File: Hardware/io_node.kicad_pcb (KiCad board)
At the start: 2 copper layers, 60 x 90 mm, 135 parts, among them J1 Conn_01x09, J10 Conn_01x04, J2 Conn_01x09, J3 Conn_01x09, J4 Conn_01x05, J5 USB_B_Micro, J6 Conn_01x05, J7 Conn_01x05, J8 Conn_01x02, J9 Conn_01x04, Q1 2N7002, Q2 2N7002, Q3 2N7002, Q4 2N7002, Q5 2N7002, Q6 2N7002, Q7 2N7002, Q8 2N7002, U1 STM32F103RBT6, U10 EL357N-G, U11 EL357N-G, U12 EL357N-G, U13 EL357N-G, U14 EL357N-G, U15 USBLC6-2SC6, U2 AMS1117-5.0, U3 AMS1117-3.3, U4 SP3485EN, U5 LM324DT, U6 LM324DT, U7 EL357N-G, U8 EL357N-G, U9 EL357N-G, Y1 8 MHz

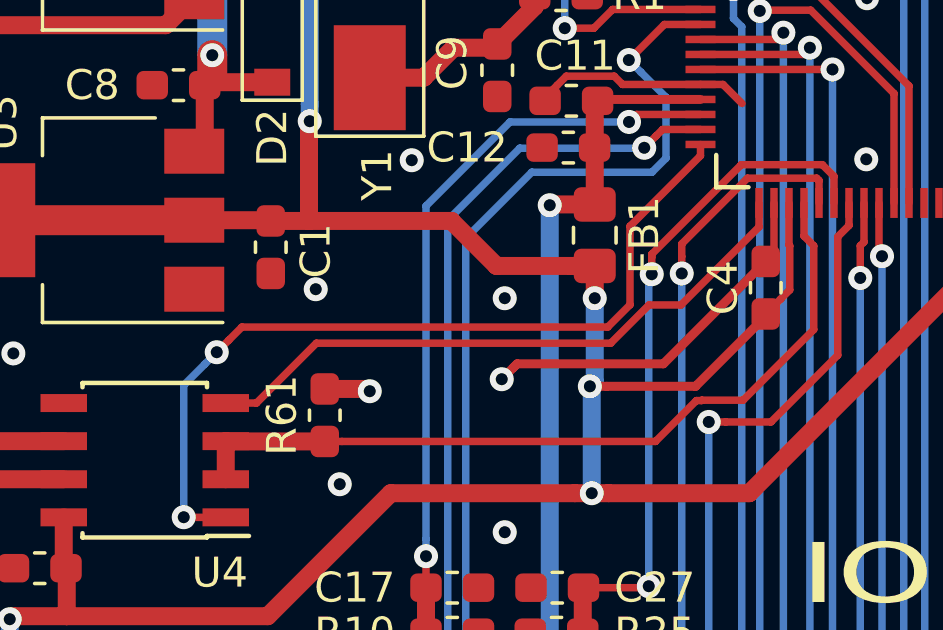
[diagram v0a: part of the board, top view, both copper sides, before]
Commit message: RS485 TX and RX was incorrect
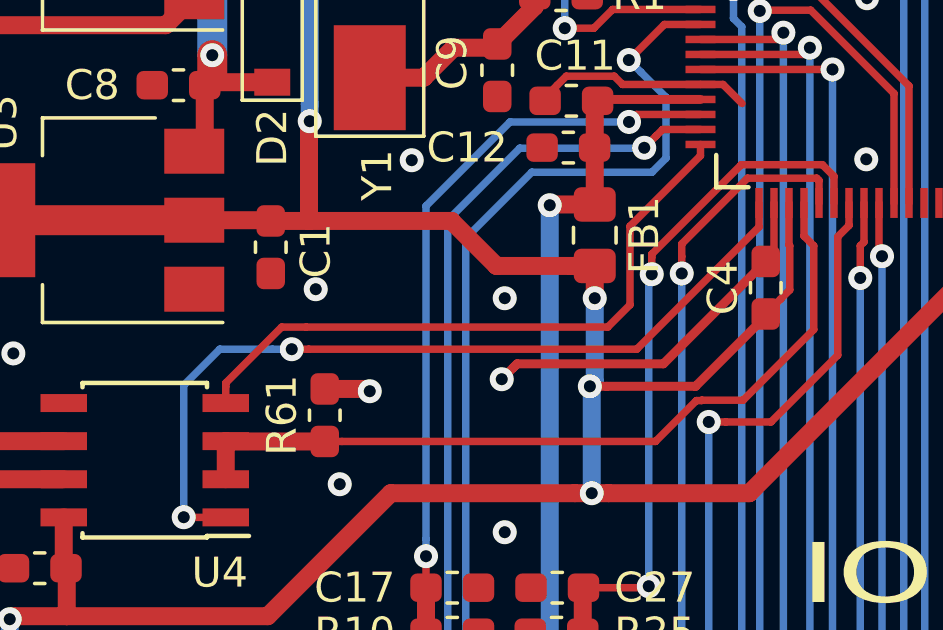
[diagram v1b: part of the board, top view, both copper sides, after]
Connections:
- U4 pad 1: /USART2_TX -> /USART2_RX
- U4 pad 4: /USART2_RX -> /USART2_TX
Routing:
- net /USART2_RX: track 21.0 -> 28.0 mm, vias 0 -> 2
- net /USART2_TX: track 28.1 -> 21.5 mm, vias 2 -> 0
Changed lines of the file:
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@@
     (fp_line (start -2.075 -2.525) (end -3.475 -2.525) (layer F.SilkS) (width 0.15))
     (pad 1 smd rect (at -2.7 -1.905 180) (size 1.55 0.6) (layers F.Cu F.Paste F.Mask)
-      (net 19 /USART2_TX))
+      (net 20 /USART2_RX))
     (pad 2 smd rect (at -2.7 -0.635 180) (size 1.55 0.6) (layers F.Cu F.Paste F.Mask)
       (net 21 /USART2_DE))
@@
       (net 21 /USART2_DE))
     (pad 4 smd rect (at -2.7 1.905 180) (size 1.55 0.6) (layers F.Cu F.Paste F.Mask)
-      (net 20 /USART2_RX))
+      (net 19 /USART2_TX))
     (pad 5 smd rect (at 2.7 1.905 180) (size 1.55 0.6) (layers F.Cu F.Paste F.Mask)
       (net 1 GND))
@@
   (segment (start 51.64 45.865) (end 51.25 45.475) (width 0.6) (layer F.Cu) (net 18))
   (segment (start 54.3 45.865) (end 51.64 45.865) (width 0.6) (layer F.Cu) (net 18))
-  (segment (start 58.305 48.405) (end 58.3 48.4) (width 0.25) (layer F.Cu) (net 19))
-  (segment (start 59.7 48.405) (end 58.305 48.405) (width 0.25) (layer F.Cu) (net 19))
-  (via (at 58.3 48.4) (size 0.8) (drill 0.4) (layers F.Cu B.Cu) (net 19))
-  (via (at 59.4 42.9) (size 0.8) (drill 0.4) (layers F.Cu B.Cu) (net 19))
-  (segment (start 75.525001 36.350001) (end 73.175172 38.69983) (width 0.25) (layer F.Cu) (net 19))
-  (segment (start 59.799999 42.500001) (end 59.4 42.9) (width 0.25) (layer F.Cu) (net 19))
-  (segment (start 60.237339 42.062661) (end 59.799999 42.500001) (width 0.25) (layer F.Cu) (net 19))
-  (segment (start 58.3 48.4) (end 58.3 44) (width 0.25) (layer B.Cu) (net 19))
-  (segment (start 59.000001 43.299999) (end 59.4 42.9) (width 0.25) (layer B.Cu) (net 19))
-  (segment (start 72.433131 42.062661) (end 60.237339 42.062661) (width 0.25) (layer F.Cu) (net 19))
   (segment (start 75.525001 35.975001) (end 75.525001 36.350001) (width 0.25) (layer F.Cu) (net 19))
-  (segment (start 73.175172 38.69983) (end 73.175172 41.32062) (width 0.25) (layer F.Cu) (net 19))
+  (segment (start 72.433131 42.062661) (end 62.38103 42.062661) (width 0.25) (layer F.Cu) (net 19))
   (segment (start 73.175172 41.32062) (end 72.433131 42.062661) (width 0.25) (layer F.Cu) (net 19))
-  (segment (start 58.3 44) (end 59.000001 43.299999) (width 0.25) (layer B.Cu) (net 19))
-  (segment (start 60.725 44.595) (end 59.7 44.595) (width 0.25) (layer F.Cu) (net 20))
-  (segment (start 62.72 42.6) (end 60.725 44.595) (width 0.25) (layer F.Cu) (net 20))
-  (segment (start 73.807225 41.324977) (end 72.532203 42.6) (width 0.25) (layer F.Cu) (net 20))
-  (segment (start 77.475001 38.724999) (end 74.875023 41.324977) (width 0.25) (layer F.Cu) (net 20))
+  (segment (start 73.175172 38.69983) (end 73.175172 41.32062) (width 0.25) (layer F.Cu) (net 19))
+  (segment (start 75.525001 36.350001) (end 73.175172 38.69983) (width 0.25) (layer F.Cu) (net 19))
+  (segment (start 59.7 44.045) (end 59.7 44.595) (width 0.25) (layer F.Cu) (net 19))
+  (segment (start 59.7 43.926998) (end 59.7 44.045) (width 0.25) (layer F.Cu) (net 19))
+  (segment (start 61.564337 42.062661) (end 59.7 43.926998) (width 0.25) (layer F.Cu) (net 19))
+  (segment (start 62.38103 42.062661) (end 61.564337 42.062661) (width 0.25) (layer F.Cu) (net 19))
+  (segment (start 59.7 48.405) (end 58.305 48.405) (width 0.25) (layer F.Cu) (net 20))
+  (segment (start 58.305 48.405) (end 58.3 48.4) (width 0.25) (layer F.Cu) (net 20))
+  (via (at 58.3 48.4) (size 0.8) (drill 0.4) (layers F.Cu B.Cu) (net 20))
+  (via (at 61.9 42.8) (size 0.8) (drill 0.4) (layers F.Cu B.Cu) (net 20))
   (segment (start 77.475001 37.925001) (end 77.475001 38.724999) (width 0.25) (layer F.Cu) (net 20))
-  (segment (start 74.875023 41.324977) (end 73.807225 41.324977) (width 0.25) (layer F.Cu) (net 20))
-  (segment (start 72.532203 42.6) (end 62.72 42.6) (width 0.25) (layer F.Cu) (net 20))
+  (segment (start 77.475001 38.724999) (end 73.4 42.8) (width 0.25) (layer F.Cu) (net 20))
+  (segment (start 62.465685 42.8) (end 61.9 42.8) (width 0.25) (layer F.Cu) (net 20))
+  (segment (start 73.4 42.8) (end 62.465685 42.8) (width 0.25) (layer F.Cu) (net 20))
+  (segment (start 61.25 42.8) (end 61.9 42.8) (width 0.25) (layer B.Cu) (net 20))
+  (segment (start 59.5 42.8) (end 61.25 42.8) (width 0.25) (layer B.Cu) (net 20))
+  (segment (start 58.3 48.4) (end 58.3 44) (width 0.25) (layer B.Cu) (net 20))
+  (segment (start 58.3 44) (end 59.5 42.8) (width 0.25) (layer B.Cu) (net 20))
   (segment (start 59.7 45.865) (end 59.7 47.135) (width 0.6) (layer F.Cu) (net 21))
   (segment (start 59.71 45.875) (end 59.7 45.865) (width 0.6) (layer F.Cu) (net 21))

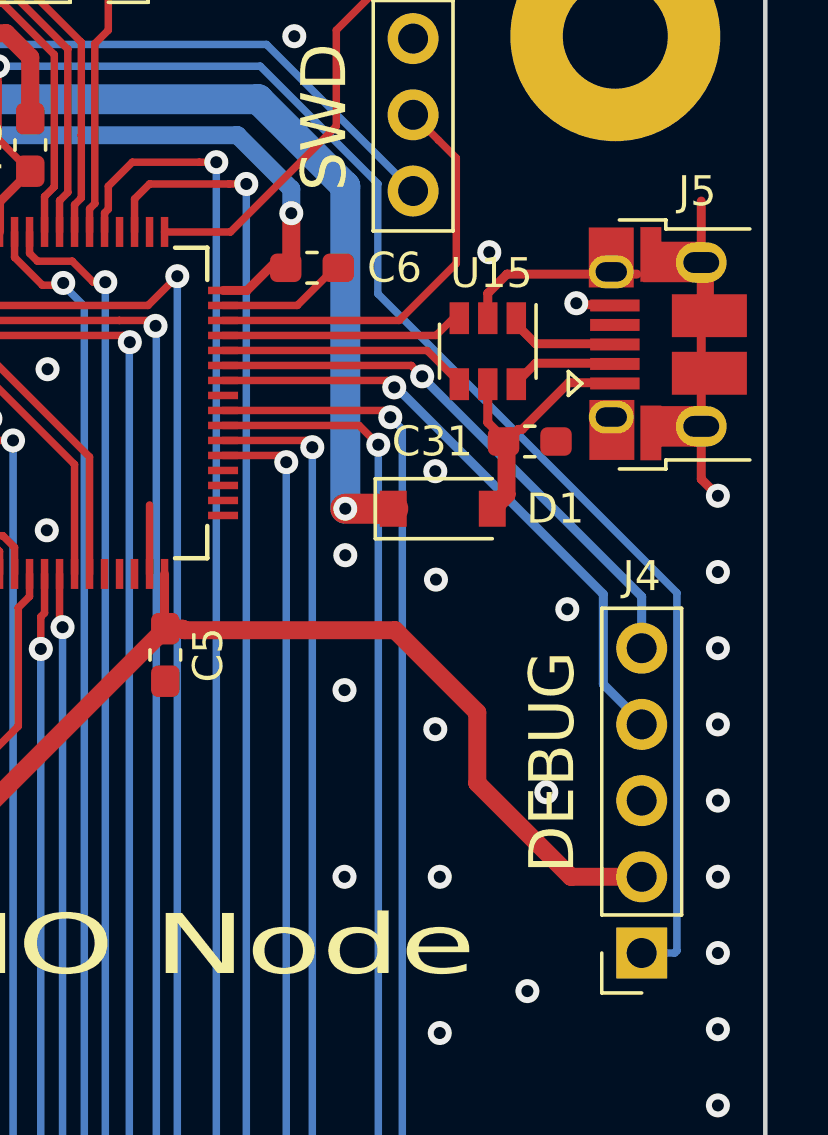
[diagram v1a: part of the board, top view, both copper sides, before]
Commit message: Debug RX TX swapped
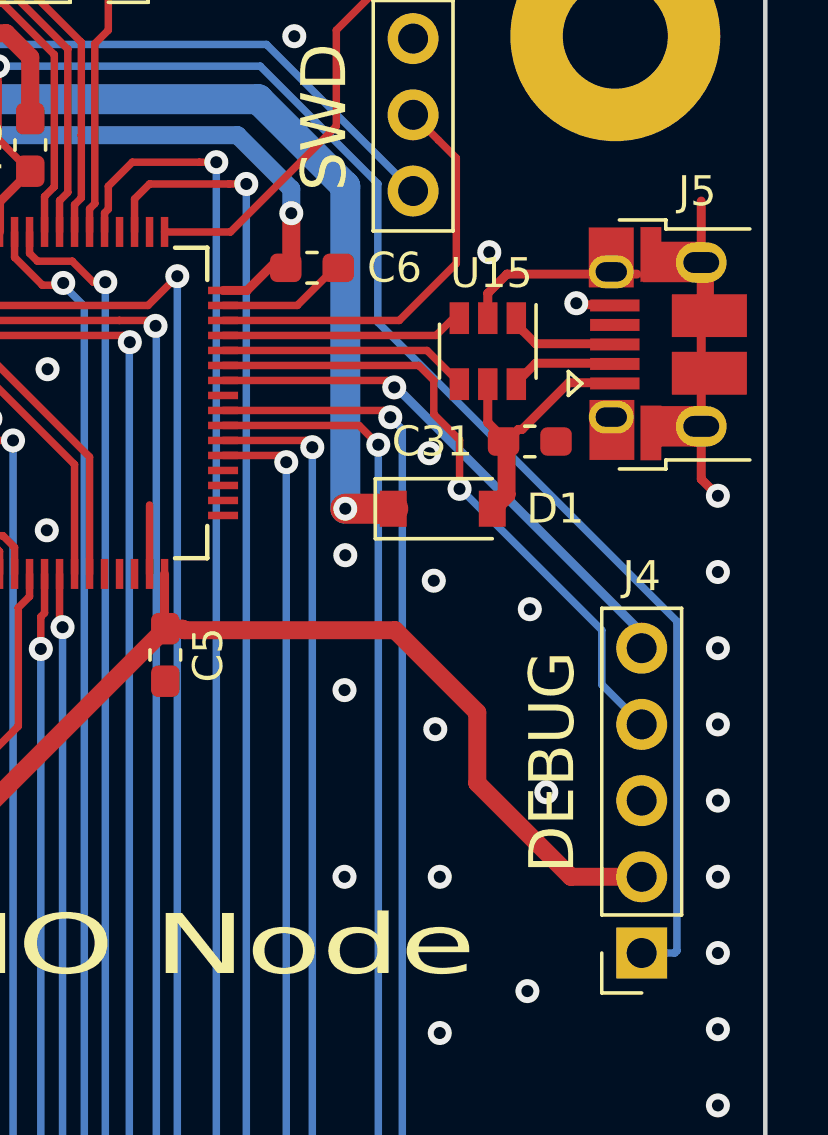
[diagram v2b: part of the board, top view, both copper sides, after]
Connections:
- J4 pad 4: /USART1_TX -> /USART1_RX
- J4 pad 5: /USART1_RX -> /USART1_TX
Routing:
- net /USART1_RX: track 18.9 -> 21.7 mm
- net /USART1_TX: track 20.5 -> 18.0 mm
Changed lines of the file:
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@@
     (thickness 1.6)
     (drawings 64)
-    (tracks 1105)
+    (tracks 1109)
     (zones 0)
     (modules 135)
@@
       (net 1 GND))
     (pad 4 thru_hole oval (at 0 7.62 180) (size 1.7 1.7) (drill 1) (layers *.Cu *.Mask)
-      (net 22 /USART1_TX))
-    (pad 5 thru_hole oval (at 0 10.16 180) (size 1.7 1.7) (drill 1) (layers *.Cu *.Mask)
       (net 23 /USART1_RX))
+    (pad 5 thru_hole oval (at 0 10.16 180) (size 1.7 1.7) (drill 1) (layers *.Cu *.Mask)
+      (net 22 /USART1_TX))
     (model ${KISYS3DMOD}/Connector_PinSocket_2.54mm.3dshapes/PinSocket_1x05_P2.54mm_Vertical.wrl
       (at (xyz 0 0 0))
@@
   (via (at 94.1 58.9) (size 0.8) (drill 0.4) (layers F.Cu B.Cu) (net 1))
   (via (at 94 43.1) (size 0.8) (drill 0.4) (layers F.Cu B.Cu) (net 1))
-  (via (at 94 34.5) (size 0.8) (drill 0.4) (layers F.Cu B.Cu) (net 1))
-  (via (at 98.4 39.1) (size 0.8) (drill 0.4) (layers F.Cu B.Cu) (net 1))
+  (via (at 93.8 33.9) (size 0.8) (drill 0.4) (layers F.Cu B.Cu) (net 1))
+  (via (at 97.15 39.1) (size 0.8) (drill 0.4) (layers F.Cu B.Cu) (net 1))
   (via (at 97.7 45.2) (size 0.8) (drill 0.4) (layers F.Cu B.Cu) (net 1))
   (segment (start 84.475001 37.925001) (end 84.475001 35.624999) (width 0.25) (layer F.Cu) (net 1))
@@
   (via (at 90.974 48.02) (size 0.8) (drill 0.4) (layers F.Cu B.Cu) (net 1))
   (via (at 90.974 41.797) (size 0.8) (drill 0.4) (layers F.Cu B.Cu) (net 1))
-  (via (at 94.022 38.114) (size 0.8) (drill 0.4) (layers F.Cu B.Cu) (net 1))
+  (via (at 93.95 38.15) (size 0.8) (drill 0.4) (layers F.Cu B.Cu) (net 1))
   (via (at 94.022 65.292) (size 0.8) (drill 0.4) (layers F.Cu B.Cu) (net 1))
   (segment (start 102.865 27.545) (end 102.865 33.005) (width 0.3) (layer F.Cu) (net 1))
@@
   (segment (start 86.925001 31.475001) (end 92.401716 31.475001) (width 0.25) (layer F.Cu) (net 22))
   (segment (start 92.401716 31.475001) (end 92.63262 31.705905) (width 0.25) (layer F.Cu) (net 22))
-  (segment (start 100.88 42.88) (end 100.88 42.94) (width 0.3) (layer B.Cu) (net 22))
-  (segment (start 99.6 41.6) (end 100.88 42.88) (width 0.3) (layer B.Cu) (net 22))
-  (segment (start 99.6 38.6) (end 99.6 41.6) (width 0.3) (layer B.Cu) (net 22))
+  (segment (start 100.88 39.88) (end 100.88 40.4) (width 0.3) (layer B.Cu) (net 22))
   (segment (start 92.63262 31.705905) (end 92.705905 31.705905) (width 0.3) (layer B.Cu) (net 22))
-  (segment (start 92.705905 31.705905) (end 99.6 38.6) (width 0.3) (layer B.Cu) (net 22))
-  (via (at 93.562348 31.337653) (size 0.8) (drill 0.4) (layers F.Cu B.Cu) (net 23))
-  (segment (start 86.925001 30.975001) (end 93.199696 30.975001) (width 0.25) (layer F.Cu) (net 23))
-  (segment (start 93.199696 30.975001) (end 93.562348 31.337653) (width 0.25) (layer F.Cu) (net 23))
-  (segment (start 100.88 38.68) (end 100.88 40.4) (width 0.3) (layer B.Cu) (net 23))
-  (segment (start 93.562348 31.337653) (end 93.562348 31.362348) (width 0.3) (layer B.Cu) (net 23))
-  (segment (start 93.562348 31.362348) (end 100.88 38.68) (width 0.3) (layer B.Cu) (net 23))
+  (segment (start 92.705905 31.705905) (end 100.88 39.88) (width 0.3) (layer B.Cu) (net 22))
+  (segment (start 100.88 42.88) (end 100.88 42.94) (width 0.3) (layer B.Cu) (net 23))
+  (via (at 94.808738 35.088173) (size 0.8) (drill 0.4) (layers F.Cu B.Cu) (net 23))
+  (segment (start 94.808738 33.458738) (end 94.808738 35.088173) (width 0.25) (layer F.Cu) (net 23))
+  (segment (start 93.95 32.6) (end 94.808738 33.458738) (width 0.25) (layer F.Cu) (net 23))
+  (segment (start 93.95 31.475305) (end 93.95 32.6) (width 0.25) (layer F.Cu) (net 23))
+  (segment (start 86.925001 30.975001) (end 93.449696 30.975001) (width 0.25) (layer F.Cu) (net 23))
+  (segment (start 93.449696 30.975001) (end 93.95 31.475305) (width 0.25) (layer F.Cu) (net 23))
+  (segment (start 99.55 41.61) (end 100.88 42.94) (width 0.25) (layer B.Cu) (net 23))
+  (segment (start 99.55 39.8) (end 99.55 41.61) (width 0.25) (layer B.Cu) (net 23))
+  (segment (start 94.846911 35.096911) (end 99.55 39.8) (width 0.25) (layer B.Cu) (net 23))
+  (segment (start 94.808738 35.088173) (end 94.8 35.096911) (width 0.25) (layer B.Cu) (net 23))
+  (segment (start 94.8 35.096911) (end 94.846911 35.096911) (width 0.25) (layer B.Cu) (net 23))
   (segment (start 66.3 55.19) (end 66.3 56.46) (width 0.6) (layer F.Cu) (net 24))
   (segment (start 66.3 52.325) (end 66.375 52.25) (width 0.6) (layer F.Cu) (net 24))
@@
   (via (at 79.425011 21) (size 0.8) (drill 0.4) (layers F.Cu B.Cu) (net 76))
   (segment (start 101.98 50.56) (end 100.88 50.56) (width 0.25) (layer B.Cu) (net 76))
-  (segment (start 79.425011 21) (end 88.16674 21) (width 0.25) (layer B.Cu) (net 76))
-  (segment (start 92.084999 24.918259) (end 92.084999 28.584999) (width 0.25) (layer B.Cu) (net 76))
-  (segment (start 92.084999 28.584999) (end 102.055001 38.555001) (width 0.25) (layer B.Cu) (net 76))
-  (segment (start 102.055001 38.555001) (end 102.055001 50.484999) (width 0.25) (layer B.Cu) (net 76))
   (segment (start 88.16674 21) (end 92.084999 24.918259) (width 0.25) (layer B.Cu) (net 76))
+  (segment (start 79.425011 21) (end 88.16674 21) (width 0.25) (layer B.Cu) (net 76))
+  (segment (start 92.084999 24.918259) (end 92.084999 29.534999) (width 0.25) (layer B.Cu) (net 76))
+  (segment (start 92.084999 29.534999) (end 102.055001 39.505001) (width 0.25) (layer B.Cu) (net 76))
+  (segment (start 102.055001 39.505001) (end 102.055001 50.484999) (width 0.25) (layer B.Cu) (net 76))
   (segment (start 102.055001 50.484999) (end 101.98 50.56) (width 0.25) (layer B.Cu) (net 76))
   (segment (start 79.583897 18.9) (end 76.84 18.9) (width 0.25) (layer F.Cu) (net 77))

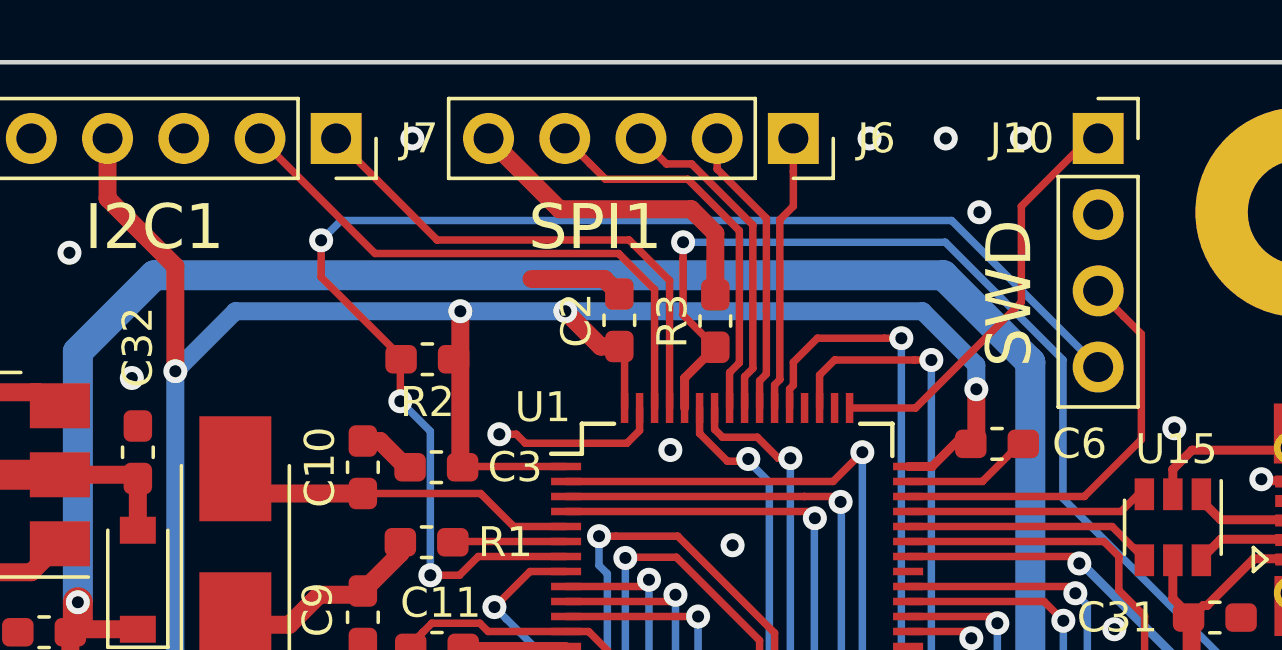
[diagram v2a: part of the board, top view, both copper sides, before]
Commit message: Add Vbat
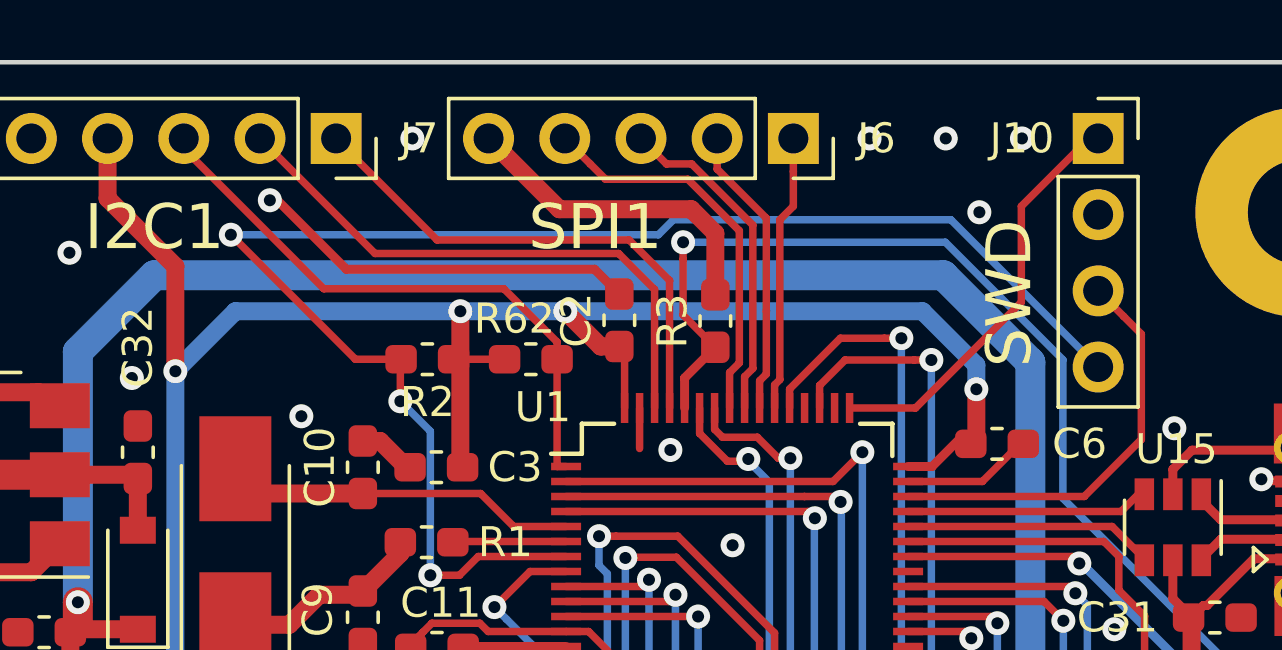
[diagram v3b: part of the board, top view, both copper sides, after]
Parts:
- added R62: 0R, Resistor_SMD:R_0603_1608Metric_Pad1.05x0.95mm_HandSolder, F.Cu at (74.3, 24.9)
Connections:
- J7 pad 3: Net-(J7-Pad3) -> +BATT
- U1 pad 1: +3V3 -> +BATT
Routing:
- net +BATT: track 0.00 -> 19.9 mm
- net GND: track 147.6 -> 153.0 mm, vias 135 -> 136
- net /NRST: track 45.7 -> 51.0 mm
- net +3V3: track 272.7 -> 270.9 mm
